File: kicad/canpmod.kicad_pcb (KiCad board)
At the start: 2 copper layers, 37.6 x 18.5 mm, 12 parts, among them J1 Conn_01x02, J2 PMOD, U1 SN65HVD230

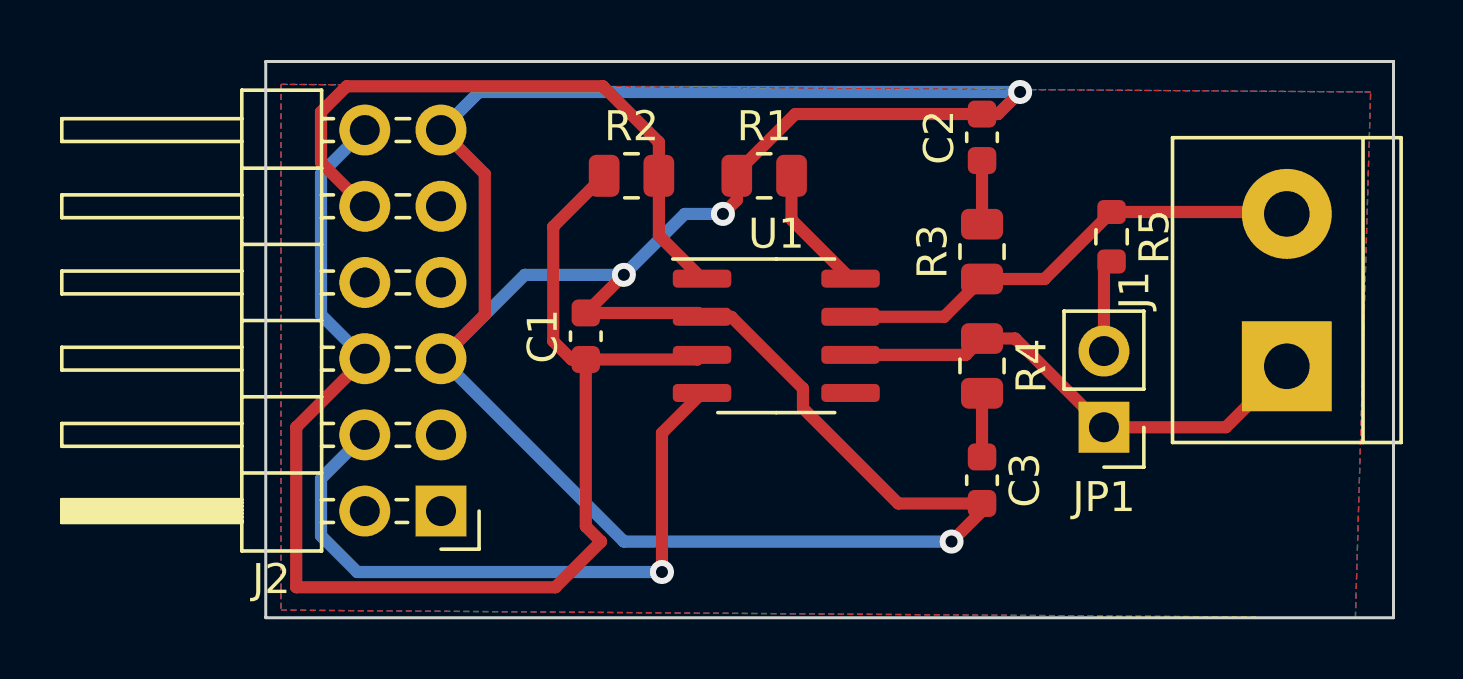
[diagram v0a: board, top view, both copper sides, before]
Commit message: Update project to Kicad 9
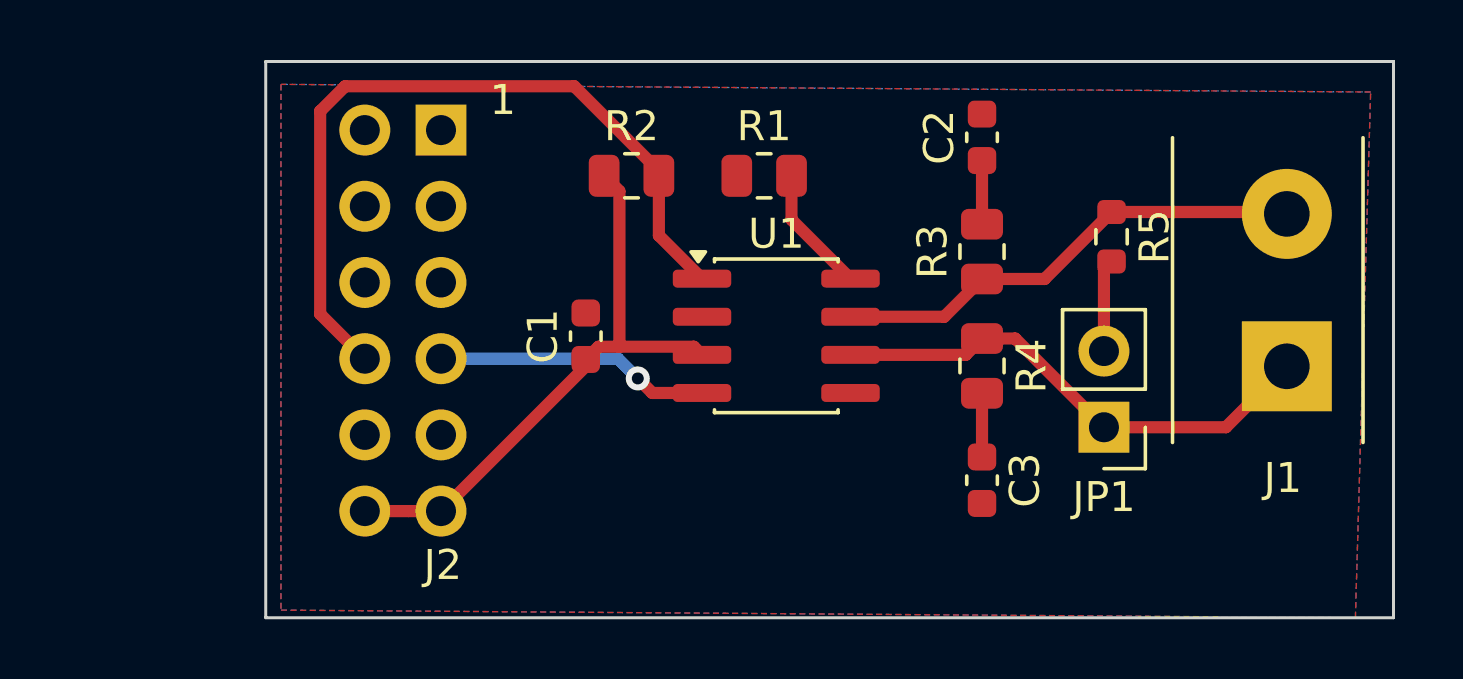
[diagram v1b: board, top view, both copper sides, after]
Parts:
- J1: footprint TerminalBlock:TerminalBlock_bornier-2_P5.08mm -> canpmod:TerminalBlock_bornier-2_P5.08mm
- J2: footprint Connector_PinHeader_2.54mm:PinHeader_2x06_P2.54mm_Horizontal -> canpmod:PMOD_2x06_Horizontal
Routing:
- net GND: track 91.4 -> 0.00 mm, vias 4 -> 0
- net +3.3V: track 46.0 -> 19.7 mm
- net CRX: track 22.4 -> 9.17 mm
- net CTX: track 21.3 -> 25.9 mm
